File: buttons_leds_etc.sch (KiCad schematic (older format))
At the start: 10 parts, among them SW2 SW_Push, SW3 SW_Push

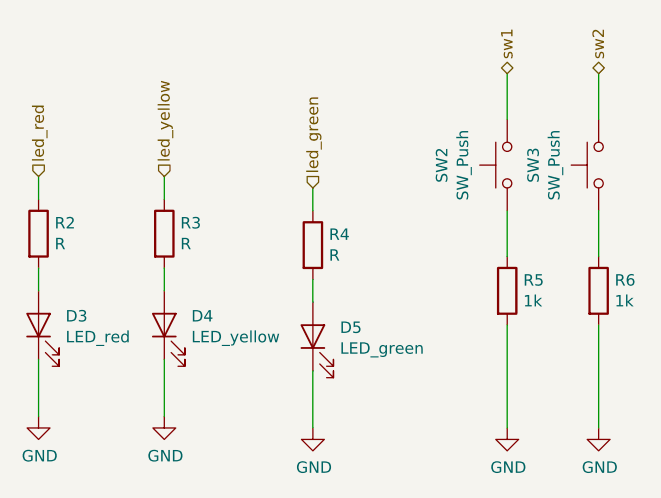
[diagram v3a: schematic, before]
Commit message: wyciecie przy gnieździe jack - dodanie 3d gniazda, update jpg
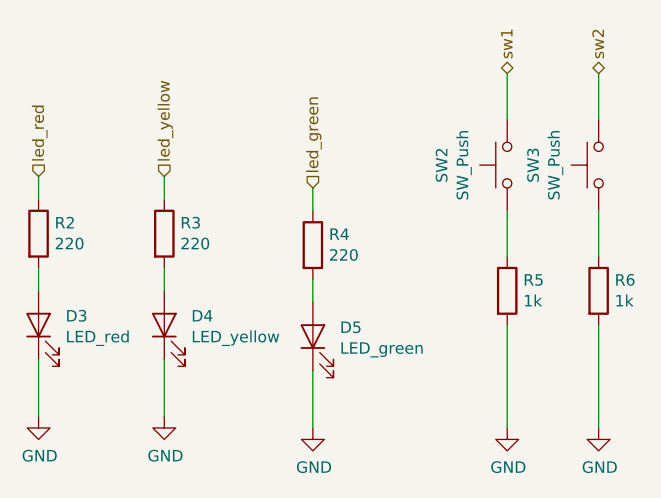
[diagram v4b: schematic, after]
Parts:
- R2, R3, R4: value R -> 220
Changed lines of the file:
@@
 P 2250 2650
 F 0 "R2" H 2320 2696 50  0000 L CNN
-F 1 "R" H 2320 2605 50  0000 L CNN
+F 1 "220" H 2320 2605 50  0000 L CNN
 F 2 "Resistor_SMD:R_0603_1608Metric" V 2180 2650 50  0001 C CNN
 F 3 "~" H 2250 2650 50  0001 C CNN
@@
 P 2800 2650
 F 0 "R3" H 2870 2696 50  0000 L CNN
-F 1 "R" H 2870 2605 50  0000 L CNN
+F 1 "220" H 2870 2605 50  0000 L CNN
 F 2 "Resistor_SMD:R_0603_1608Metric" V 2730 2650 50  0001 C CNN
 F 3 "~" H 2800 2650 50  0001 C CNN
@@
 P 3450 2700
 F 0 "R4" H 3520 2746 50  0000 L CNN
-F 1 "R" H 3520 2655 50  0000 L CNN
+F 1 "220" H 3520 2655 50  0000 L CNN
 F 2 "Resistor_SMD:R_0603_1608Metric" V 3380 2700 50  0001 C CNN
 F 3 "~" H 3450 2700 50  0001 C CNN

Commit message: update front endu do termopary i przełącznika zasilającego
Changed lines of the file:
@@
 Wire Wire Line
 	3450 2950 3450 2850
-Text HLabel 2250 2400 1    50   Input ~ 0
+Text HLabel 2250 2400 1    50   Input ~ 6
 led_red
 Wire Wire Line
 	2250 2500 2250 2400
-Text HLabel 2800 2400 1    50   Input ~ 0
+Text HLabel 2800 2400 1    50   Input ~ 6
 led_yellow
 Wire Wire Line
 	2800 2400 2800 2500
-Text HLabel 3450 2450 1    50   Input ~ 0
+Text HLabel 3450 2450 1    50   Input ~ 6
 led_green
 Wire Wire Line
@@
 Wire Wire Line
 	4700 3500 4700 3050
-Text HLabel 4300 1950 1    50   BiDi ~ 0
+Text HLabel 4300 1950 1    50   BiDi ~ 6
 sw1
 Wire Wire Line
 	4300 2150 4300 1950
-Text HLabel 4700 1950 1    50   BiDi ~ 0
+Text HLabel 4700 1950 1    50   BiDi ~ 6
 sw2
 Wire Wire Line
